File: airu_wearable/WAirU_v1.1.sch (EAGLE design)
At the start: 57 parts, among them Q1 BSS123, Q2 MMBT3904LT1G, Q3 MMBT3904LT1G, Q4 BSS84, U1 19-237A/BHR6GHC-M01/2T, U2 CN3065-DFN8, U3 HDC1080DMBT, U4 PAM2305AABADJ, U6 PAM2401, U7 ESP32_WROOM32_SKINNY

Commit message: PCB design
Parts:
- C10: value 10uf -> 22uf; device OPL_Capacitor:CERAMIC-10UF-10V-10%-X5R(0603) -> Seeed-OPL-Capacitor:CERAMIC-22UF-6.3V-20%-X5R(0805)
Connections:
- net N$67 renamed V_IN1
- removed net 5.0V: C2.2, C3.2, MOLEX-53261-0871-8.S
- net VBUS: now also C2.2, C3.2, MOLEX-53261-0871-8.S
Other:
- moved on the sheet: L2
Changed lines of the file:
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@@
 <part name="U$12" library="ESP32" deviceset="VBUS" device=""/>
 <part name="U2" library="Seeed-IC" deviceset="PMIC-CN3065(DFN8)" device="" value="CN3065-DFN8"/>
-<part name="C10" library="OPL_Capacitor" deviceset="CERAMIC-10UF-10V-10%-X5R(0603)" device="" package3d_urn="urn:adsk.eagle:package:8004287/1" value="10uf"/>
 <part name="U$18" library="Power or GND " deviceset="GND_POWER" device=""/>
 <part name="U$20" library="Power or GND " deviceset="GND_POWER" device=""/>
@@
 <part name="U$31" library="Power or GND " deviceset="GND_POWER" device=""/>
 <part name="U$32" library="Power or GND " deviceset="GND_POWER" device=""/>
+<part name="C10" library="Seeed-OPL-Capacitor" deviceset="CERAMIC-22UF-6.3V-20%-X5R(0805)" device="" value="22uf"/>
 </parts>
 <sheets>
@@
 </segment>
 </net>
-<net name="5.0V" class="0">
-<segment>
-<pinref part="U$56" gate="G$1" pin="5.0V"/>
-<pinref part="C3" gate="G$1" pin="2"/>
-<wire x1="93.98" y1="162.56" x2="93.98" y2="161.29" width="0.1524" layer="91"/>
-</segment>
-<segment>
-<pinref part="U$58" gate="G$1" pin="5.0V"/>
-<pinref part="C2" gate="G$1" pin="2"/>
-<wire x1="86.36" y1="162.56" x2="86.36" y2="161.29" width="0.1524" layer="91"/>
+<net name="PMS_TX" class="0">
+<segment>
+<pinref part="R4" gate="G$1" pin="2"/>
+<wire x1="107.95" y1="144.78" x2="134.62" y2="144.78" width="0.1524" layer="91"/>
+<pinref part="MOLEX-53261-0871" gate="-4" pin="S"/>
+<label x="121.92" y="144.78" size="1.778" layer="95"/>
+</segment>
+</net>
+<net name="TXD0" class="0">
+<segment>
+<pinref part="MOLEX-53261-0871" gate="-5" pin="S"/>
+<wire x1="134.62" y1="147.32" x2="121.92" y2="147.32" width="0.1524" layer="91"/>
+<label x="121.92" y="147.32" size="1.778" layer="95"/>
+</segment>
+<segment>
+<pinref part="U7" gate="G$1" pin="TXD0"/>
+<wire x1="27.94" y1="66.04" x2="10.16" y2="66.04" width="0.1524" layer="91"/>
+<label x="10.16" y="66.04" size="1.778" layer="95"/>
+</segment>
+</net>
+<net name="VBUS" class="0">
+<segment>
+<wire x1="214.63" y1="85.09" x2="217.17" y2="85.09" width="0.1524" layer="91"/>
+<pinref part="L3" gate="L" pin="2"/>
+<label x="217.17" y="85.09" size="1.778" layer="95"/>
 </segment>
 <segment>
@@
 <pinref part="MOLEX-53261-0871" gate="-8" pin="S"/>
 <wire x1="116.84" y1="154.94" x2="134.62" y2="154.94" width="0.1524" layer="91"/>
-<label x="124.46" y="154.94" size="1.778" layer="95"/>
-</segment>
-</net>
-<net name="PMS_TX" class="0">
-<segment>
-<pinref part="R4" gate="G$1" pin="2"/>
-<wire x1="107.95" y1="144.78" x2="134.62" y2="144.78" width="0.1524" layer="91"/>
-<pinref part="MOLEX-53261-0871" gate="-4" pin="S"/>
-<label x="121.92" y="144.78" size="1.778" layer="95"/>
-</segment>
-</net>
-<net name="TXD0" class="0">
-<segment>
-<pinref part="MOLEX-53261-0871" gate="-5" pin="S"/>
-<wire x1="134.62" y1="147.32" x2="121.92" y2="147.32" width="0.1524" layer="91"/>
-<label x="121.92" y="147.32" size="1.778" layer="95"/>
-</segment>
-<segment>
-<pinref part="U7" gate="G$1" pin="TXD0"/>
-<wire x1="27.94" y1="66.04" x2="10.16" y2="66.04" width="0.1524" layer="91"/>
-<label x="10.16" y="66.04" size="1.778" layer="95"/>
-</segment>
-</net>
-<net name="VBUS" class="0">
-<segment>
-<wire x1="214.63" y1="85.09" x2="217.17" y2="85.09" width="0.1524" layer="91"/>
-<pinref part="L3" gate="L" pin="2"/>
-<label x="217.17" y="85.09" size="1.778" layer="95"/>
+<label x="121.92" y="154.94" size="1.778" layer="95"/>
+</segment>
+<segment>
+<pinref part="U$58" gate="G$1" pin="5.0V"/>
+<pinref part="C2" gate="G$1" pin="2"/>
+<wire x1="86.36" y1="162.56" x2="86.36" y2="161.29" width="0.1524" layer="91"/>
+<label x="78.74" y="160.02" size="1.778" layer="95"/>
+</segment>
+<segment>
+<pinref part="U$56" gate="G$1" pin="5.0V"/>
+<pinref part="C3" gate="G$1" pin="2"/>
+<wire x1="93.98" y1="162.56" x2="93.98" y2="161.29" width="0.1524" layer="91"/>
+<label x="101.6" y="162.56" size="1.778" layer="95" rot="R180"/>
 </segment>
 </net>
@@
 <attribute name="VALUE" x="187.96" y="113.03" size="1.27" layer="96" ratio="10"/>
 </instance>
-<instance part="C10" gate="G$1" x="163.83" y="98.298" smashed="yes" rot="R90">
-<attribute name="NAME" x="162.56" y="94.488" size="1.27" layer="95" ratio="10" rot="R90"/>
-<attribute name="VALUE" x="166.37" y="94.488" size="1.27" layer="96" ratio="10" rot="R90"/>
-</instance>
 <instance part="U$18" gate="G$1" x="187.96" y="96.52" smashed="yes"/>
 <instance part="U$20" gate="G$1" x="208.28" y="93.98" smashed="yes"/>
@@
 <attribute name="VALUE" x="60.706" y="94.742" size="1.27" layer="96" ratio="10"/>
 </instance>
-<instance part="L2" gate="G$1" x="82.042" y="90.17" smashed="yes">
-<attribute name="NAME" x="79.502" y="91.44" size="1.27" layer="95" ratio="10"/>
-<attribute name="VALUE" x="79.502" y="87.63" size="1.27" layer="96" ratio="10"/>
+<instance part="L2" gate="G$1" x="84.582" y="90.17" smashed="yes">
+<attribute name="NAME" x="82.042" y="91.44" size="1.27" layer="95" ratio="10"/>
+<attribute name="VALUE" x="82.042" y="87.63" size="1.27" layer="96" ratio="10"/>
 </instance>
 <instance part="R12" gate="G$1" x="162.56" y="142.24" smashed="yes" rot="R90">
@@
 <instance part="U$31" gate="G$1" x="22.86" y="120.65" smashed="yes"/>
 <instance part="U$32" gate="G$1" x="163.83" y="92.202" smashed="yes"/>
+<instance part="C10" gate="G$1" x="163.83" y="98.298" smashed="yes" rot="R90">
+<attribute name="NAME" x="162.56" y="96.012" size="1.27" layer="95" ratio="10" rot="R90"/>
+<attribute name="VALUE" x="166.37" y="95.758" size="1.27" layer="96" ratio="10" rot="R90"/>
+</instance>
 </instances>
 <busses>
@@
 </segment>
 <segment>
-<pinref part="C10" gate="G$1" pin="1"/>
 <pinref part="U$32" gate="G$1" pin="GND"/>
 <wire x1="163.83" y1="94.488" x2="163.83" y2="92.202" width="0.1524" layer="91"/>
+<pinref part="C10" gate="G$1" pin="1"/>
 </segment>
 </net>
@@
 <pinref part="TP_3V3" gate="G$1" pin="TP"/>
 <pinref part="C12" gate="G$1" pin="2"/>
-<wire x1="87.122" y1="90.17" x2="92.71" y2="90.17" width="0.1524" layer="91"/>
+<wire x1="89.662" y1="90.17" x2="92.71" y2="90.17" width="0.1524" layer="91"/>
 <wire x1="92.71" y1="90.17" x2="96.012" y2="90.17" width="0.1524" layer="91"/>
 <wire x1="96.012" y1="90.17" x2="101.092" y2="90.17" width="0.1524" layer="91"/>
@@
 <pinref part="U2" gate="G$1" pin="VIN"/>
 <wire x1="176.53" y1="102.87" x2="163.83" y2="102.87" width="0.1524" layer="91"/>
-<pinref part="C10" gate="G$1" pin="2"/>
 <wire x1="163.83" y1="102.108" x2="163.83" y2="102.87" width="0.1524" layer="91"/>
 <junction x="163.83" y="102.87"/>
+<pinref part="C10" gate="G$1" pin="2"/>
 </segment>
 </net>
@@
 <pinref part="U4" gate="G$1" pin="VOUT"/>
 <pinref part="L2" gate="G$1" pin="1"/>
+<wire x1="79.502" y1="90.17" x2="76.962" y2="90.17" width="0.1524" layer="91"/>
 </segment>
 </net>
@@
 </segment>
 </net>
-<net name="N$67" class="0">
+<net name="V_IN1" class="0">
 <segment>
 <pinref part="L1" gate="L" pin="1"/>

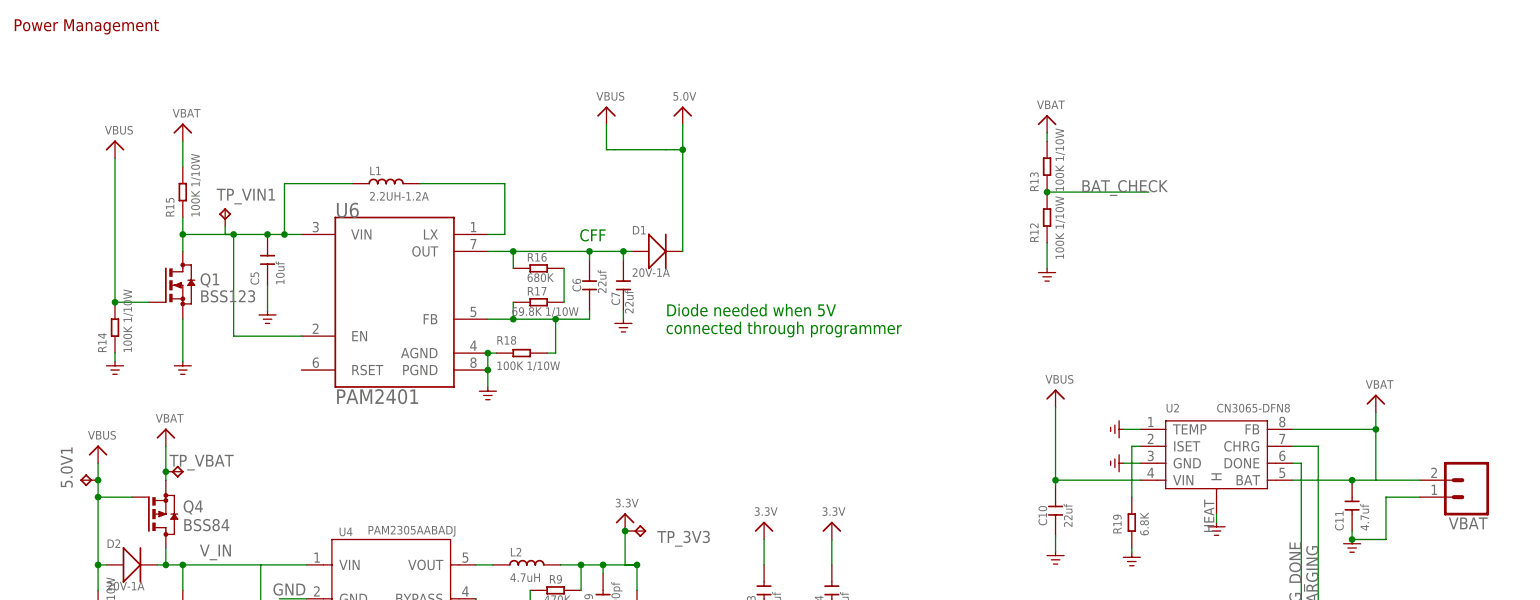
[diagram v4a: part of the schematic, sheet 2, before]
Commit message: new issue (#16) opened. Remade PAM2401 circuit.
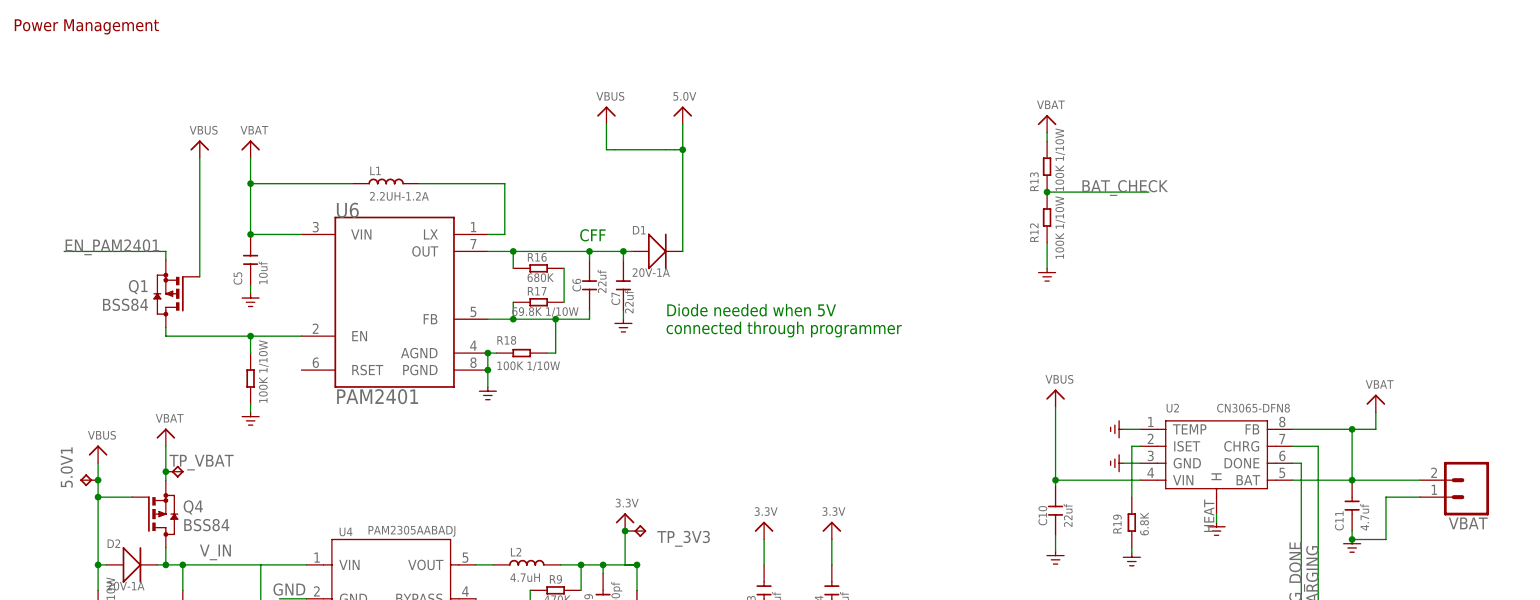
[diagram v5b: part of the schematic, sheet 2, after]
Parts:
- removed R15: 100K 1/10W, Seeed-Resistor:SMD-RES-100K-5%-1/10W(0603)
- removed TP_VIN1: TPTP20SQ, testpad:TPTP20SQ
- Q1: value BSS123 -> BSS84; device transistor-small-signal:BSS123 -> BSS84:BSS84
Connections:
- removed net PM_RESET: MOLEX-53261-0871-3.S, R3.2, U7.IO2/A2_2
- removed net PM_SET/RXD0: MOLEX-53261-0871-6.S, U7.IO4/A2_0, U7.RXD0
- new net EN_PAM2401: Q1.S, U7.IO2/A2_2
- new net N$7: Q1.D, R14.2, U6.EN
- new net PM_SET: MOLEX-53261-0871-6.S, R3.2, U7.IO4/A2_0
- new net RXD0: MOLEX-53261-0871-3.S, U7.RXD0
- net GND: no longer Q1.S
- net VBAT: no longer R15.2
- net VBUS: no longer R14.2
- net V_IN1: no longer Q1.D, R15.1, TP_VIN1.TP, U6.EN
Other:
- note added: "PMS Prog ------- -------- - 5V - NC - GND - GND - SET - NC - NC - Prog RX - TX - NC - NC - Prog TX - NC - DTR - NC - RTS"
- note removed: "PMS-TX (UART2-RX)"
- note removed: "PM_NC / UART0-TX"
- note removed: "PM_RESET"
- note removed: "PM_SET / UART0-RX"
- note removed: "PROG-DTR"
- note removed: "PROG-RTS"
- note removed: "Remove RTS line from PMS sensor cable"
- moved on the sheet: C5

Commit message: added comment.
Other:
- note added: "Pulldown connected to VBUS on PAM2305 circuit, so not needed here"
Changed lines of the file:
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@@
 <text x="105.41" y="127" size="1.778" layer="91" align="center-left">Diode needed when 5V
 connected through programmer</text>
+<text x="35.56" y="146.05" size="1.016" layer="91" align="bottom-right">Pulldown connected to
+VBUS on PAM2305 circuit,
+so not needed here</text>
 </plain>
 <instances>

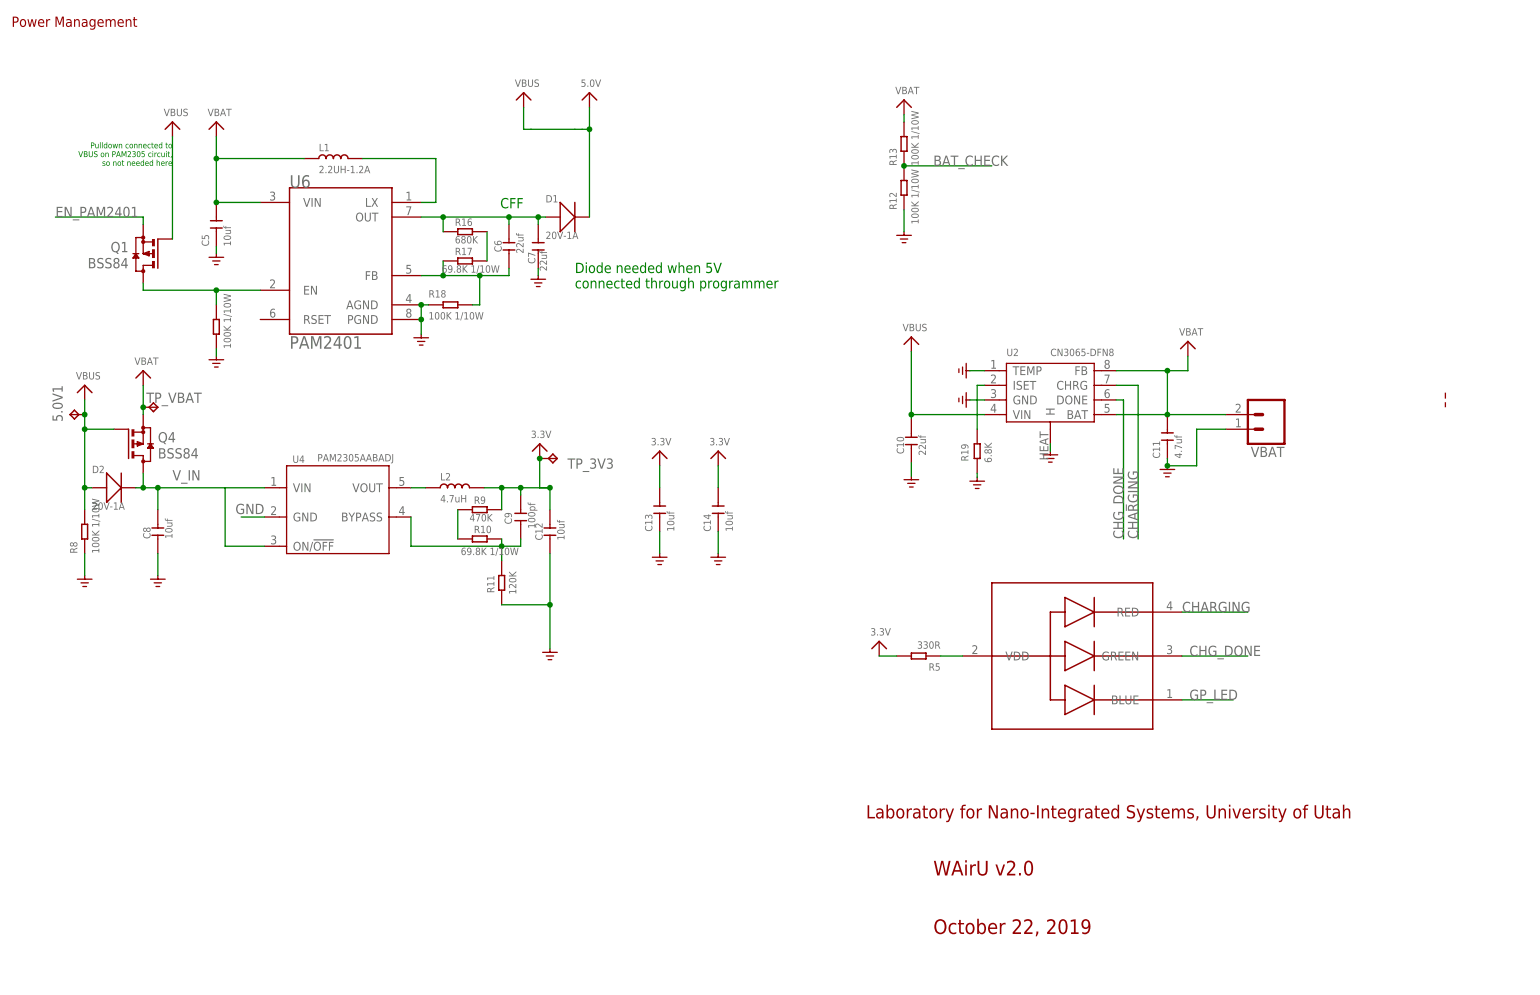
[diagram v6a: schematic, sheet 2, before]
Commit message: Draw PCB plus dimension for WAirU 2.1 Export BOM list Included PCB pdf for future references
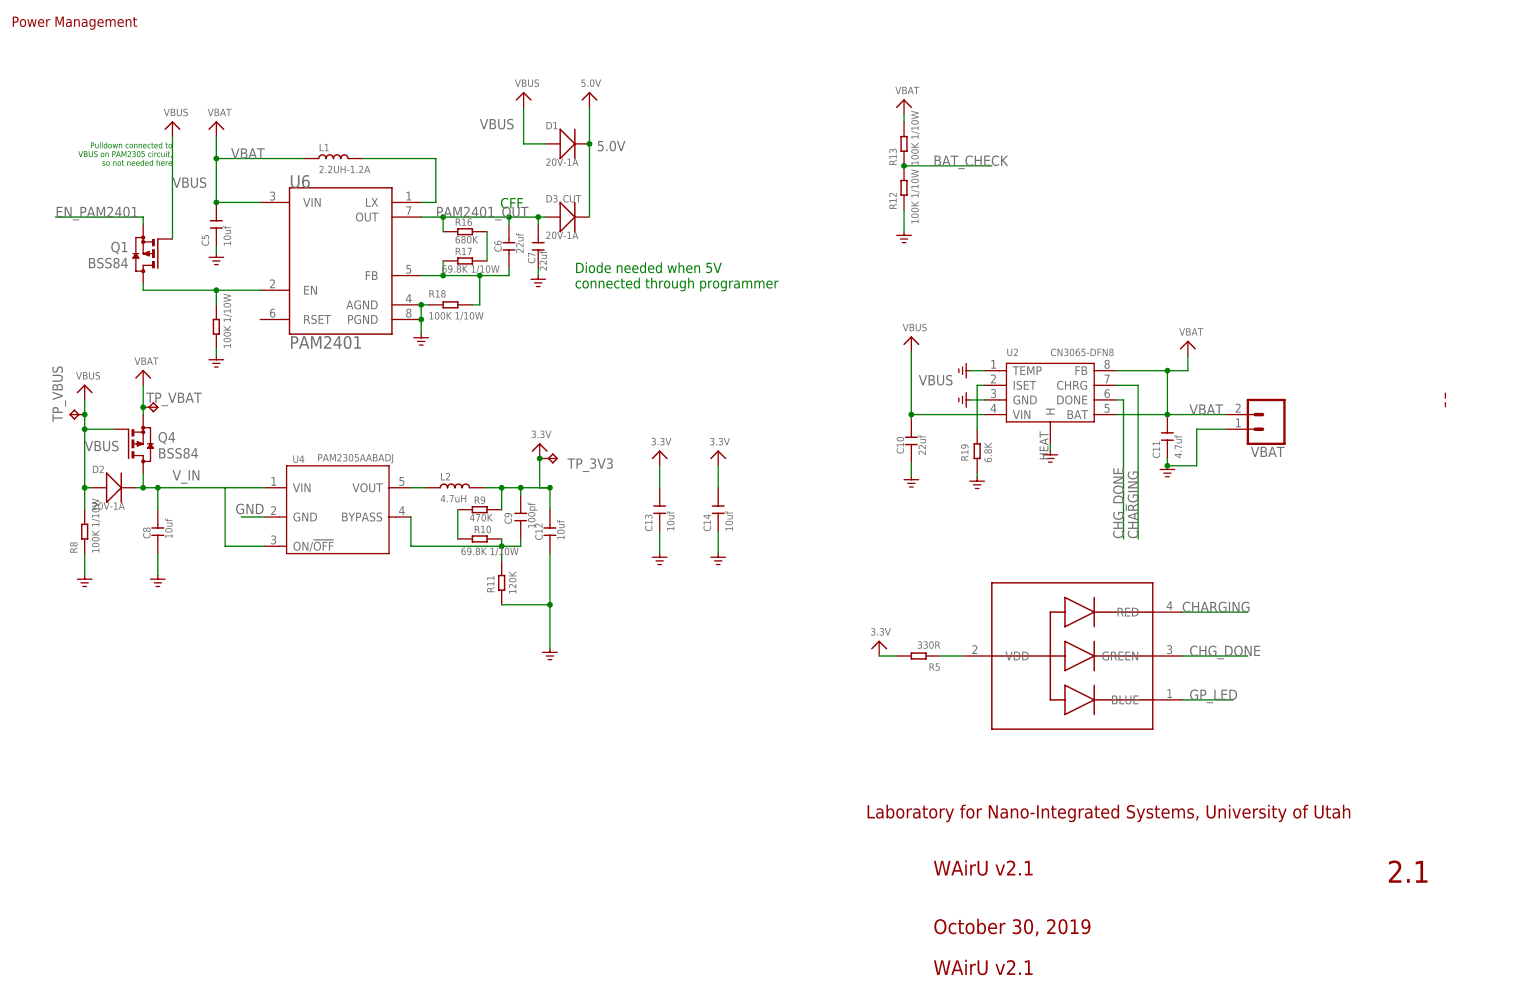
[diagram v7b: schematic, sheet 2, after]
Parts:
- added D3_CUT: 20V-1A, Seeed-OPL-Diode:SMD-DIODE-SCHOTTKY-20V-1A(SOD-123)
- renumbered 5.0V1 to TP_VBUS
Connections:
- removed net N$4: C6.2, C7.2, D1.+, R16.1, U6.OUT
- removed net V_IN1: C5.2, L1.1, U6.VIN
- new net 5.0V: C2.2, C3.2, D1.-, D3_CUT.-, MOLEX-53261-0871-8.S
- new net PAM2401_OUT: C6.2, C7.2, D3_CUT.+, R16.1, U6.OUT
- net VBAT: now also C5.2, L1.1, U6.VIN
- net VBUS: now also D1.+; no longer C2.2, C3.2, D1.-, MOLEX-53261-0871-8.S
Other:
- note added: "2.1"
- note added: "October 30, 2019"
- note added: "WAirU v2.1"
- note removed: "October 22, 2019"
- note removed: "WAirU v2.0"
- moved on the sheet: D1
